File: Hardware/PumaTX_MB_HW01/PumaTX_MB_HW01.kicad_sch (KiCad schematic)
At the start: 125 parts, among them J100 FH12A-26S-0.5SH_55_, J101 FH12-12S-0.5SH_55_, J102 500334-0160, J103 500334-0160, J104 692122030100, J105 53398-0667, J400 U.FL-R-SMT-1_40_, J410 U.FL-R-SMT-1_40_, M130 Motor_DC, M140 Fan, Q130 ZXMN3B01F, Q140 ZXMN3B01F, Q200 UMH3NTN, Q201 UMH3NTN, U200 CP2105-F01-GMR, U300 ESP32-PICO-D4, U400 ESP32-PICO-D4, U402 E28-2G4M27S, U410 SX1280, U500 BQ24075RGTR, U510 MIC5528-3.3YMT-T5, U520 MIC5528-3.3YMT-T5, U530 MIC5528-3.3YMT-T5, Y410 NX2016SA-52MHZ-EXS00A-CS06016

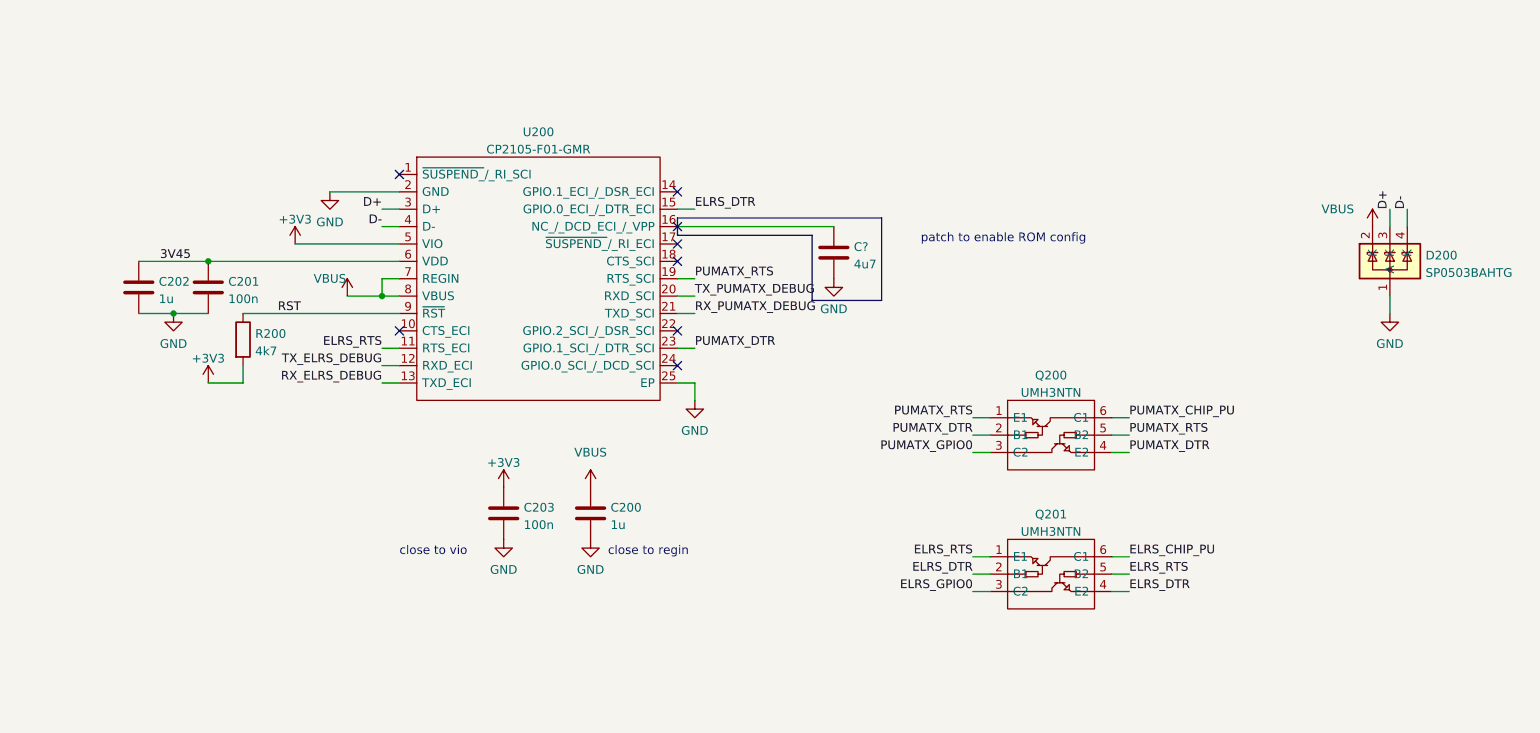
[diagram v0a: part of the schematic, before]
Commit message: created PUMATX_MB_HW01 and added patch to HW00
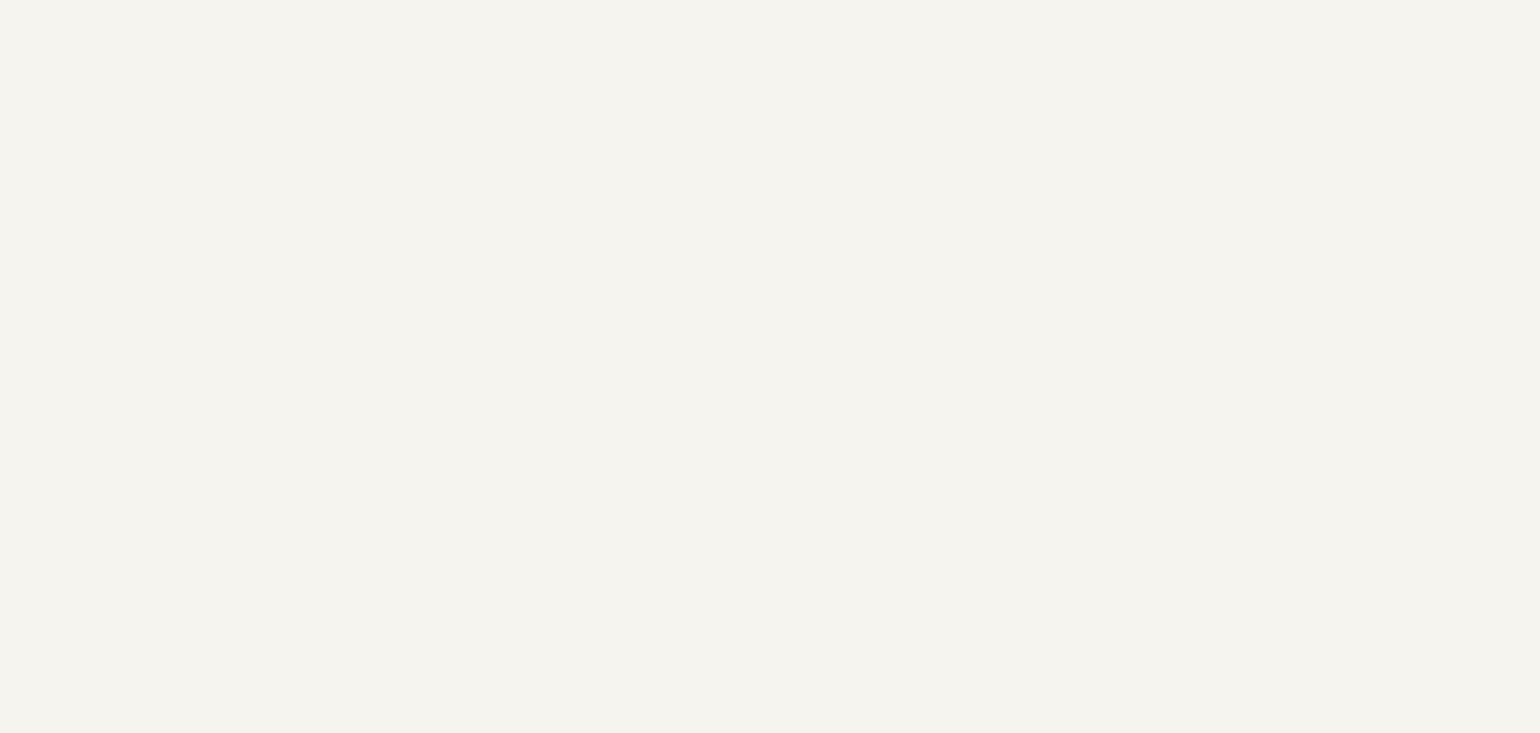
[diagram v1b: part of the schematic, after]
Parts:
- removed C200, C202: 1u, Capacitor_SMD:C_0603_1608Metric, symbol Component lib:C
- removed C201: 100n, Capacitor_SMD:C_0603_1608Metric, symbol Component lib:C
- removed C203: 100n, Capacitor_SMD:C_0402_1005Metric, symbol Component lib:C
- removed C?: 4u7, Capacitor_SMD:C_0603_1608Metric, symbol Component lib:C
- removed D200: SP0503BAHTG, Component_lib:SP0503BAHTG, symbol Component lib:SP0503BAHTG
- removed Q200, Q201: UMH3NTN, Component_lib:UMH3NTN, symbol Component_lib:UMH3NTN
- removed R200: 4k7, Capacitor_SMD:C_0402_1005Metric, symbol Component lib:R
- removed U200: CP2105-F01-GMR, Component_lib:QFN50P400X400X80-25N-D, symbol Component_lib:CP2105-F01-GMR
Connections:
- no-connect marks 44 -> 36
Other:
- note removed: "close to regin"
- note removed: "close to vio"
- note removed: "patch to enable ROM config"
- title: PumaTX_MB -> PumaTX_MB_HW01

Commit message: hw01
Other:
- note removed: "200- USB to dual UART"
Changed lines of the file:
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@@
     (effects (font (size 1.27 1.27)) (justify left bottom))
-  )
-  (text "200- USB to dual UART" (at 360.68 43.18 0)
-    (effects (font (size 5 5) (thickness 1) bold) (justify left bottom))
   )
   (text "not really -3v3,\njust convinient" (at 530.86 261.62 0)

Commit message: MB_00 schematic done
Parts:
- removed ANT300: 2450AT18A100E, Component_lib:ANTC3216X140N, symbol Component_lib:2450AT18A100E
- removed C300, C351: 1u, Capacitor_SMD:C_0402_1005Metric, symbol Component_lib:C
- removed C306, C307: C, Capacitor_SMD:C_0201_0603Metric, symbol Component_lib:C
- removed C350: 100n, Capacitor_SMD:C_0402_1005Metric, symbol Component_lib:C
- removed C352: 10u, Capacitor_SMD:C_0402_1005Metric, symbol Component_lib:C
- removed C501: 1u, Capacitor_SMD:C_0603_1608Metric, symbol Component lib:C
- removed C502, C503: 4u7, Capacitor_SMD:C_0603_1608Metric, symbol Component lib:C
- removed C510, C511: 2u2, Capacitor_SMD:C_0603_1608Metric, symbol Component lib:C
- removed D500, D501: LED, Capacitor_SMD:C_0402_1005Metric, symbol Component_lib:LED
- removed L300: L, Capacitor_SMD:C_0402_1005Metric, symbol Component_lib:L
- removed R101, R102, R510: 0k, Capacitor_SMD:C_0402_1005Metric, symbol Component_lib:R
- removed R300: 10k, Capacitor_SMD:C_0201_0603Metric, symbol Component_lib:R
- removed R305: 120k, Capacitor_SMD:C_0402_1005Metric, symbol Component lib:R
- removed R306: 470k, Capacitor_SMD:C_0402_1005Metric, symbol Component lib:R
- removed R501: 100k, Capacitor_SMD:C_0402_1005Metric, symbol Component_lib:R
- removed R502: 1k1, Capacitor_SMD:C_0402_1005Metric, symbol Component_lib:R
- removed R503: 590, Capacitor_SMD:C_0402_1005Metric, symbol Component_lib:R
- removed R504: 0, Capacitor_SMD:C_0402_1005Metric, symbol Component_lib:R
- removed R505: 36k5, Capacitor_SMD:C_0402_1005Metric, symbol Component_lib:R
- removed R506, R507: 1k5, Capacitor_SMD:C_0402_1005Metric, symbol Component_lib:R
- removed TP300: PUMATX_PU, TestPoint:TestPoint_Pad_D1.0mm, symbol Connector:TestPoint
- removed TP301: VDD_SDIO, TestPoint:TestPoint_Pad_D1.0mm, symbol Connector:TestPoint
- removed TP501: BQ_PGOOD, TestPoint:TestPoint_Pad_D1.0mm, symbol Connector:TestPoint
- removed TP502: BQ_CHG, TestPoint:TestPoint_Pad_D1.0mm, symbol Connector:TestPoint
- removed U300: ESP32-PICO-D4, Component_lib:ESP32-PICO-D4_1, symbol Component_lib:ESP32-PICO-D4
- removed U500: BQ24075RGTR, Component_lib:QFN50P300X300X100-17N-D, symbol Component lib:BQ24075RGTR
- removed U510: MIC5528-3.3YMT-T5, Component_lib:SON40P120X120X60-7N-D, symbol Component lib:MIC5528-3.3YMT-T5
- added J1: PSoM_ESP32S2_Carrier_Board, Component_lib:PSoM_ESP32S2_00, symbol Component_lib:PSoM_ESP32S2_Carrier_Board
- added JP1, JP2, JP3, JP4: Jumper_2_Small_Open, Jumper:SolderJumper-2_P1.3mm_Open_RoundedPad1.0x1.5mm, symbol Jumper:Jumper_2_Small_Open
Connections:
- net +3V3: now also J100.15, J1.18 (3V3), J1.20 (3V3), JP4.2 (B); no longer J104.3 (D+)
- net BATTERY_TEMP: now also J105.5, J1.3 (BATTERY_TEMP); no longer J105.2
- net BATTERY_WHITE: now also J105.6; no longer J105.1
- net C1: now also J1.25 (IO12)
- net C2: now also J1.27 (IO13)
- net CRSF: now also J1.21 (IO10)
- net D+: now also J1.56 (D+)
- net D-: now also J1.58 (D-)
- net DISPLAY_BACKLIGHT: now also J1.30 (IO33)
- net DISPLAY_SCL: now also J1.15 (IO7)
- net DISPLAY_SDA: now also J1.13 (IO6)
- net DOWN: now also J1.31 (IO15)
- net ELRS_CHIP_PU: now also J1.40 (IO38)
- net ELRS_GPIO0: now also J1.38 (IO37)
- net GND: now also J1.1 (GND), J1.2 (GND), J1.22 (GND), J1.24 (GND), J1.41 (GND), J1.54 (GND), J1.59 (GND), J1.60 (GND)
- net HAPTIC_PWM: now also J1.32 (IO34)
- net LED: now also J1.39 (IO21)
- net LEFT: now also J1.35 (IO17/DAC)
- net LEFT_POT: now also J1.19 (IO9)
- net OK: now also J1.37 (IO18/DAC)
- net ON_OFF: now also J1.52 (IO42)
- net PAUSE: now also J1.7 (IO3)
- net PHOTO: now also J1.11 (IO5)
- net PUMATX_CHIP_PU: now also J1.28 (RST)
- net PUMATX_GPIO0: now also J1.26 (BOOT0)
- net PUMATX_SCL: now also J1.44 (IO39)
- net PUMATX_SDA: now also J1.42 (IO41)
- net RECORD: now also J1.9 (IO4)
- net RIGHT: now also J1.33 (IO16)
- net RIGHT_POT: now also J1.17 (IO8)
- net RTH: now also J1.5 (IO2)
- net RX_ELRS_DEBUG: now also J1.36 (IO36)
- net RX_PUMATX_DEBUG: now also J1.48 (RX), JP1.2 (B)
- net SPORT: now also J1.23 (IO11)
- net TX_ELRS_DEBUG: now also J1.34 (IO35)
- net TX_PUMATX_DEBUG: now also J1.50 (TX), JP2.2 (B)
- net UP: now also J1.29 (IO14)
- net VBAT: now also J105.1, J105.2, J1.4 (VBAT), J1.6 (VBAT), J1.8 (VBAT); no longer J105.5, J105.6
- net VBUS: now also J1.10 (VBUS), J1.12 (VBUS), JP3.2 (B); no longer J104.2 (D-)
- net VSYS: now also J1.14 (VSYS), J1.16 (VSYS)
- net at J104.5 (SSRX-): now also JP2.1 (A)
- net at J104.6 (SSRX+): now also JP1.1 (A)
- new net: J104.2 (D-), JP3.1 (A)
- new net: J104.3 (D+), JP4.1 (A)
- no-connect marks 36 -> 33
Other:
- note removed: "13 GPI 4 GPO 3 ADC 2 I2C 1 UART"
- note removed: "1550/Iin=R502"
- note removed: "1u to 10u"
- note removed: "36k5: 5h safety 30min pre charge"
- note removed: "4u7 to 47u"
- note removed: "890/Ichg=R503"
- note removed: "SYSOFF low for normal operation"
- moved on the sheet: BZ100, C101, C102, C103, C110, C120, C130, C140, C301, C302, C303, C304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

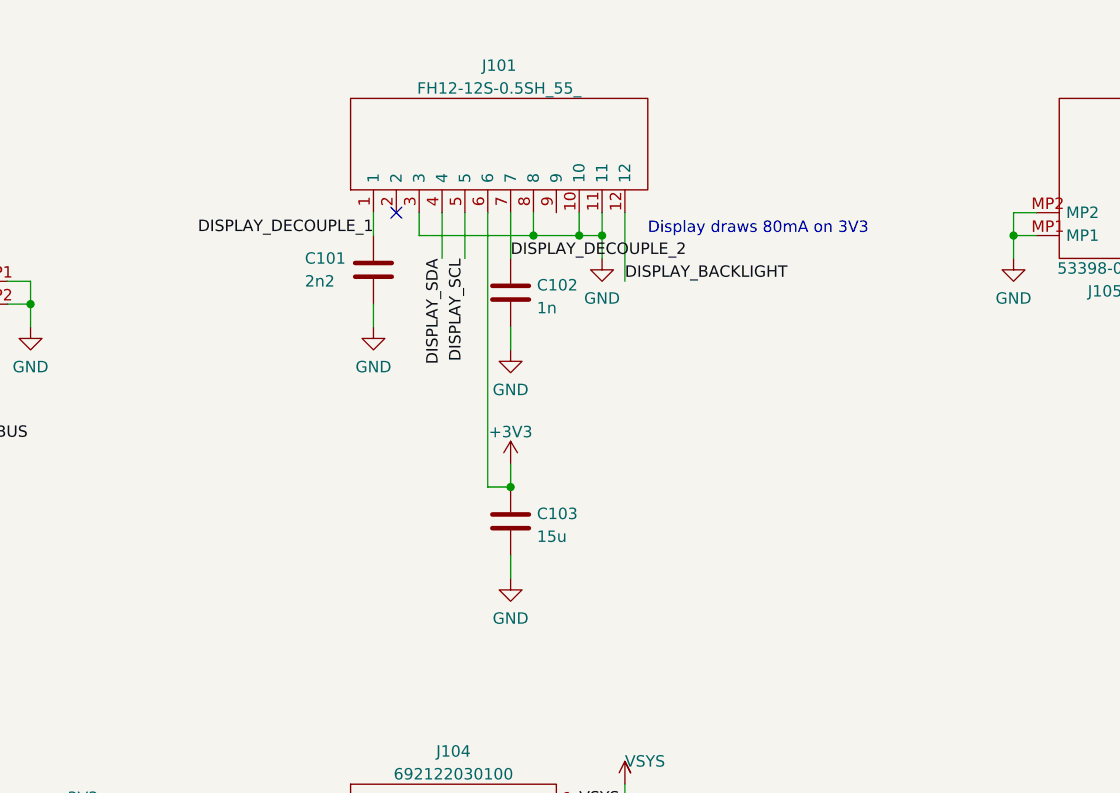
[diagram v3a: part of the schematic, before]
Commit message: updated display connector
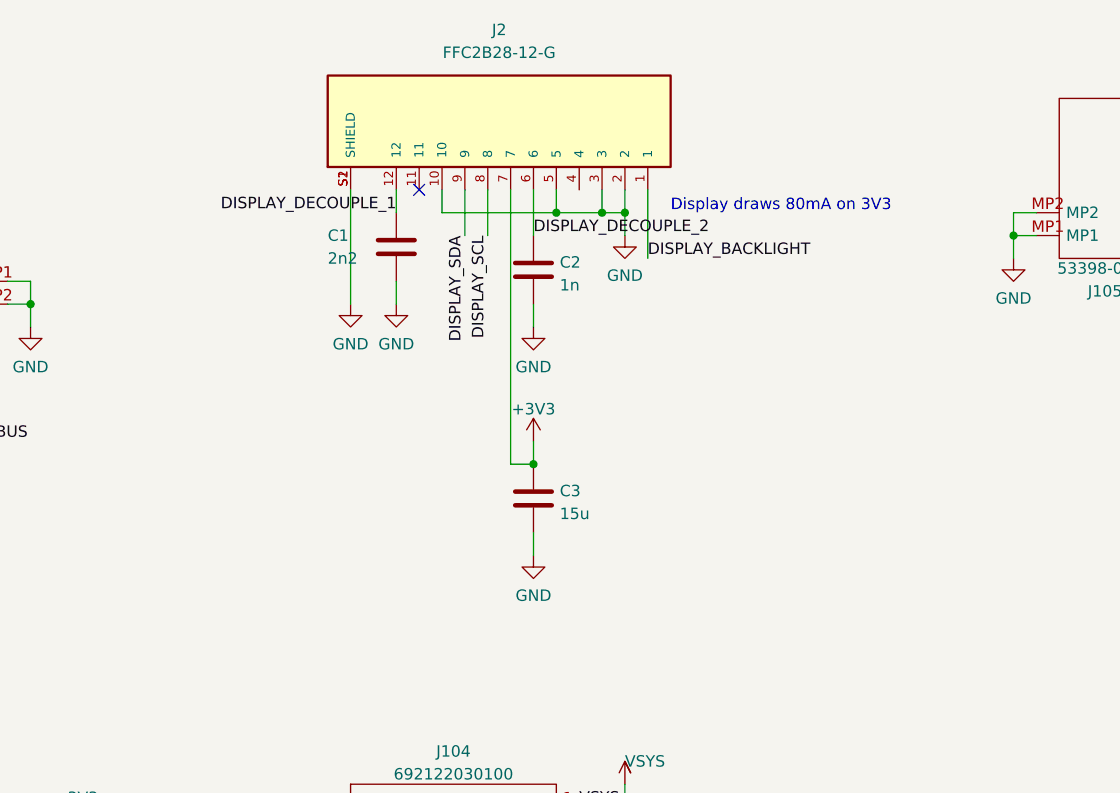
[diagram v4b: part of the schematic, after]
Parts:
- removed C101: 2n2, Capacitor_SMD:C_0402_1005Metric, symbol Component_lib:C
- removed C102: 1n, Capacitor_SMD:C_0402_1005Metric, symbol Component_lib:C
- removed C103: 15u, Capacitor_SMD:C_0402_1005Metric, symbol Component_lib:C
- removed J101: FH12-12S-0.5SH_55_, Component_lib:FH12-12S-0.5SH_55_, symbol Component_lib:FH12-12S-0.5SH_55_
- added C1: 2n2, Capacitor_SMD:C_0402_1005Metric, symbol Component_lib:C
- added C2: 1n, Capacitor_SMD:C_0402_1005Metric, symbol Component_lib:C
- added C3: 15u, Capacitor_SMD:C_0402_1005Metric, symbol Component_lib:C
- added J2: FFC2B28-12-G, Component_lib:GCT_FFC2B28-12-G, symbol Component_lib:FFC2B28-12-G
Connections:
- net +3V3: now also C3.1, J2.7
- net DISPLAY_BACKLIGHT: now also J2.1
- net DISPLAY_DECOUPLE_1: now also C1.1, J2.12
- net DISPLAY_DECOUPLE_2: now also C2.1, J2.6
- net DISPLAY_SCL: now also J2.8
- net DISPLAY_SDA: now also J2.9
- net GND: now also C1.2, C2.2, C3.2, J2.10, J2.2, J2.3, J2.5, J2.S1 (SHIELD), J2.S2 (SHIELD)

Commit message: worked on mb_01 schematic
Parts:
- removed J410: U.FL-R-SMT-1_40_, Component_lib:u.fl, symbol Component lib:U.FL-R-SMT-1_40_
- removed U410: SX1280, Component_lib:QFN50P400X400X100-25N-D, symbol Component_lib:SX1280
- removed Y410: NX2016SA-52MHZ-EXS00A-CS06016, Component_lib:NX2016SA32MEXS00ACS06465, symbol Component lib:NX2016SA-52MHZ-EXS00A-CS06016
- added J3: U.FL-R-SMT-1_40_, Component_lib:u.fl, symbol Component_lib:U.FL-R-SMT-1_40_
- added U1, U2: 74HC165BQ,115, Component_lib:74HC165BQ115, symbol Component_lib:74HC165BQ115
- added U3: SX1280, Component_lib:QFN50P400X400X100-25N-D, symbol Component_lib:SX1280_sch
- added Y1: NX2016SA-52MHZ-EXS00A-CS06016, NX2016SA52MHZEXS00ACS06016, symbol Component_lib:NX2016SA-52MHZ-EXS00A-CS06016
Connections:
- net +3V3: now also U1.16 (VCC), U2.16 (VCC)
- net 50_ELRS_ANT_1: now also U3.22 (RFIO)
- net 50_ELRS_ANT_4: now also J3.1 (ant)
- net BUSY: now also U3.7 (BUSY)
- net C1: now also U1.13 (D2); no longer J1.25 (IO12)
- net C2: now also U1.12 (D1); no longer J1.27 (IO13)
- net DIO1: now also U3.8 (DIO1)
- net DIO2: now also U3.9 (DIO2)
- net DOWN: now also U2.6 (D7); no longer J1.31 (IO15)
- net GND: now also J3.2 (gnd), U1.17 (GND_2), U1.8 (GND_1), U2.17 (GND_2), U2.8 (GND_1), U3.13 (GND), U3.20 (GND), U3.21 (GND), U3.23 (GND), U3.24 (GND), U3.25 (GND), U3.5 (GND), Y1.2, Y1.4; no longer J400.3 (gnd)
- net LEFT: now also U2.4 (D5); no longer J1.35 (IO17/DAC)
- net OK: now also U2.3 (D4); no longer J1.37 (IO18/DAC)
- net PAUSE: now also U1.5 (D6); no longer J1.7 (IO3)
- net PHOTO: now also U1.3 (D4); no longer J1.11 (IO5)
- net RECORD: now also U1.4 (D5); no longer J1.9 (IO4)
- net RIGHT: now also U2.5 (D6); no longer J1.33 (IO16)
- net RTH: now also U1.6 (D7); no longer J1.5 (IO2)
- net SPORT: now also U1.14 (D3); no longer J1.23 (IO11)
- net SX1280_3V3: now also U3.11 (VBAT_IO), U3.15 (VBAT)
- net UP: now also U1.11 (D0); no longer J1.29 (IO14)
- net V_DCC: now also U3.12 (DCC_FB), U3.2 (VDD_IN)
- net V_DCC2: now also U3.14 (DCC_SW)
- net V_PA: now also U3.1 (VR_PA)
- net XTA: now also U3.4 (XTA), Y1.3
- net XTB: now also U3.6 (XTB), Y1.1
- net at R413.1: now also U3.16 (MISO_TX)
- net at R412.1: now also U3.17 (MOSI_RX)
- net at R411.1: now also U3.18 (SCK_RSTN)
- net at R410.1: now also U3.19 (NSS_CTS)
- net at R414.2: now also U3.3 (NRESET)
- new net: U1.10 (DS), U2.9 (Q7)
- new net PL: J1.23 (IO11), U1.1 (~{PL}), U2.1 (~{PL})
- new net SPI_CE: J1.11 (IO5), U1.15 (~{CE}), U2.15 (~{CE})
- new net SPI_CLK: J1.9 (IO4), U1.2 (CP), U2.2 (CP)
- new net SPI_MISO: J1.7 (IO3), U1.9 (Q7)
- new net SPI_MOSI: J1.5 (IO2)
- no-connect marks 33 -> 50
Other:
- title: PumaTX_MB_HW01 -> PumaTX_MB_01
- moved on the sheet: C301, C302, C303, C304, C410, C411, C412, C413, C414, C415, C416, C418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
